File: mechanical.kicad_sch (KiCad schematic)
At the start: 16 parts

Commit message: Cosmetic changes
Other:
- moved on the sheet: MP?

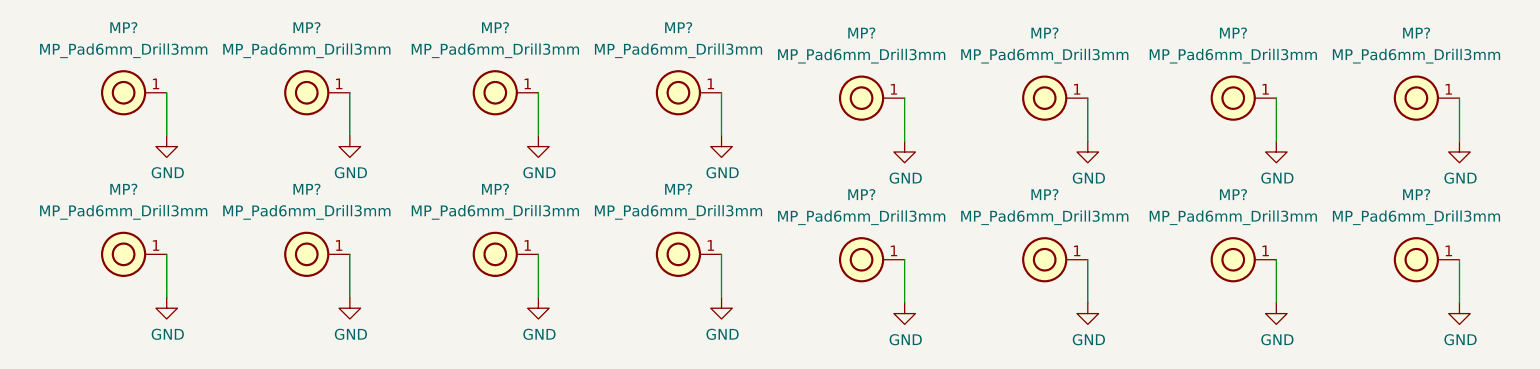
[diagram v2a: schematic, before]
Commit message: Reannotate schematic symbols
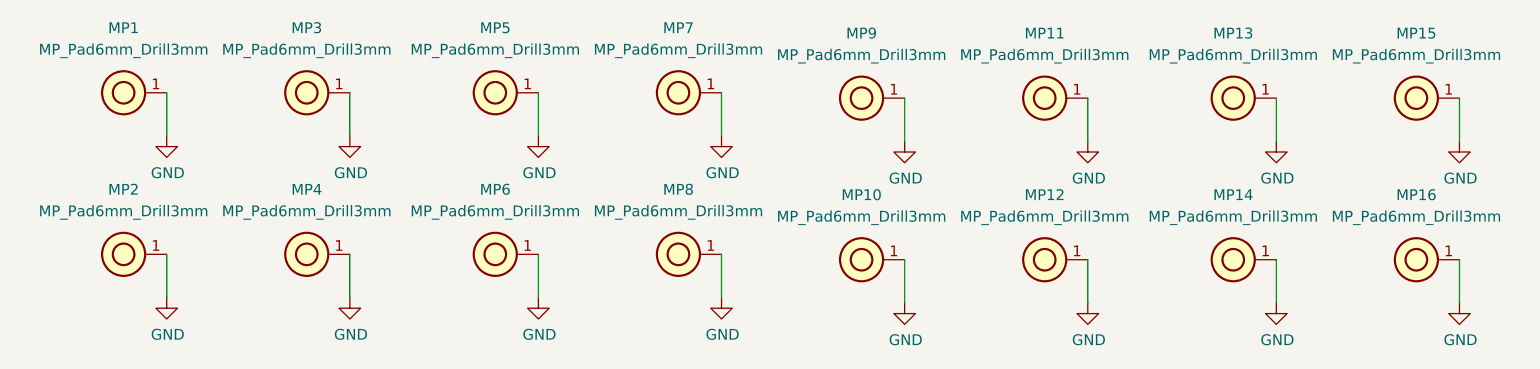
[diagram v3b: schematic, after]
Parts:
- gave numbers to parts that had none: 16

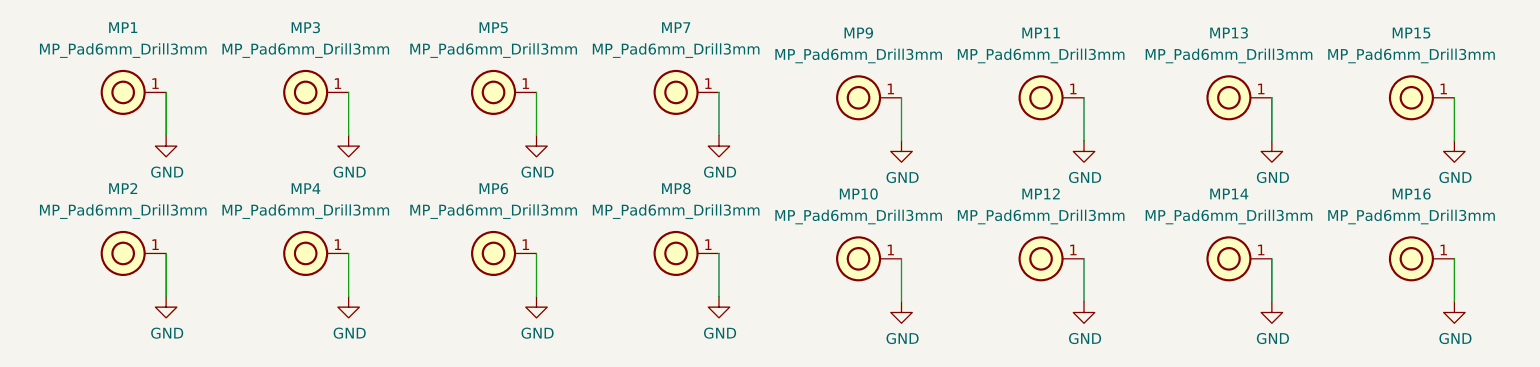
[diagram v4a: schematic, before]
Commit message: Standarize mechanicals and output control
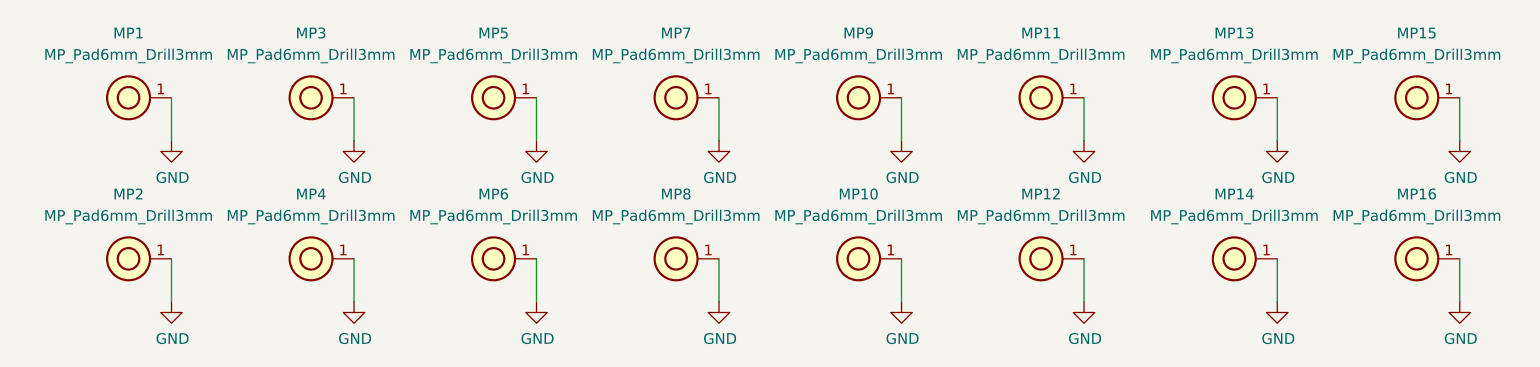
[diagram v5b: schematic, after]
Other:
- moved on the sheet: MP1, MP13, MP14, MP15, MP16, MP2, MP3, MP4, MP5, MP6, MP7, MP8
